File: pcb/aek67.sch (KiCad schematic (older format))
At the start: 20 parts, among them J1 AVR-ISP-6, SW1 SW_PUSH, U1 PRTR5V0U2X, U2 ATmega32U4-AU, X1 XTAL_GND

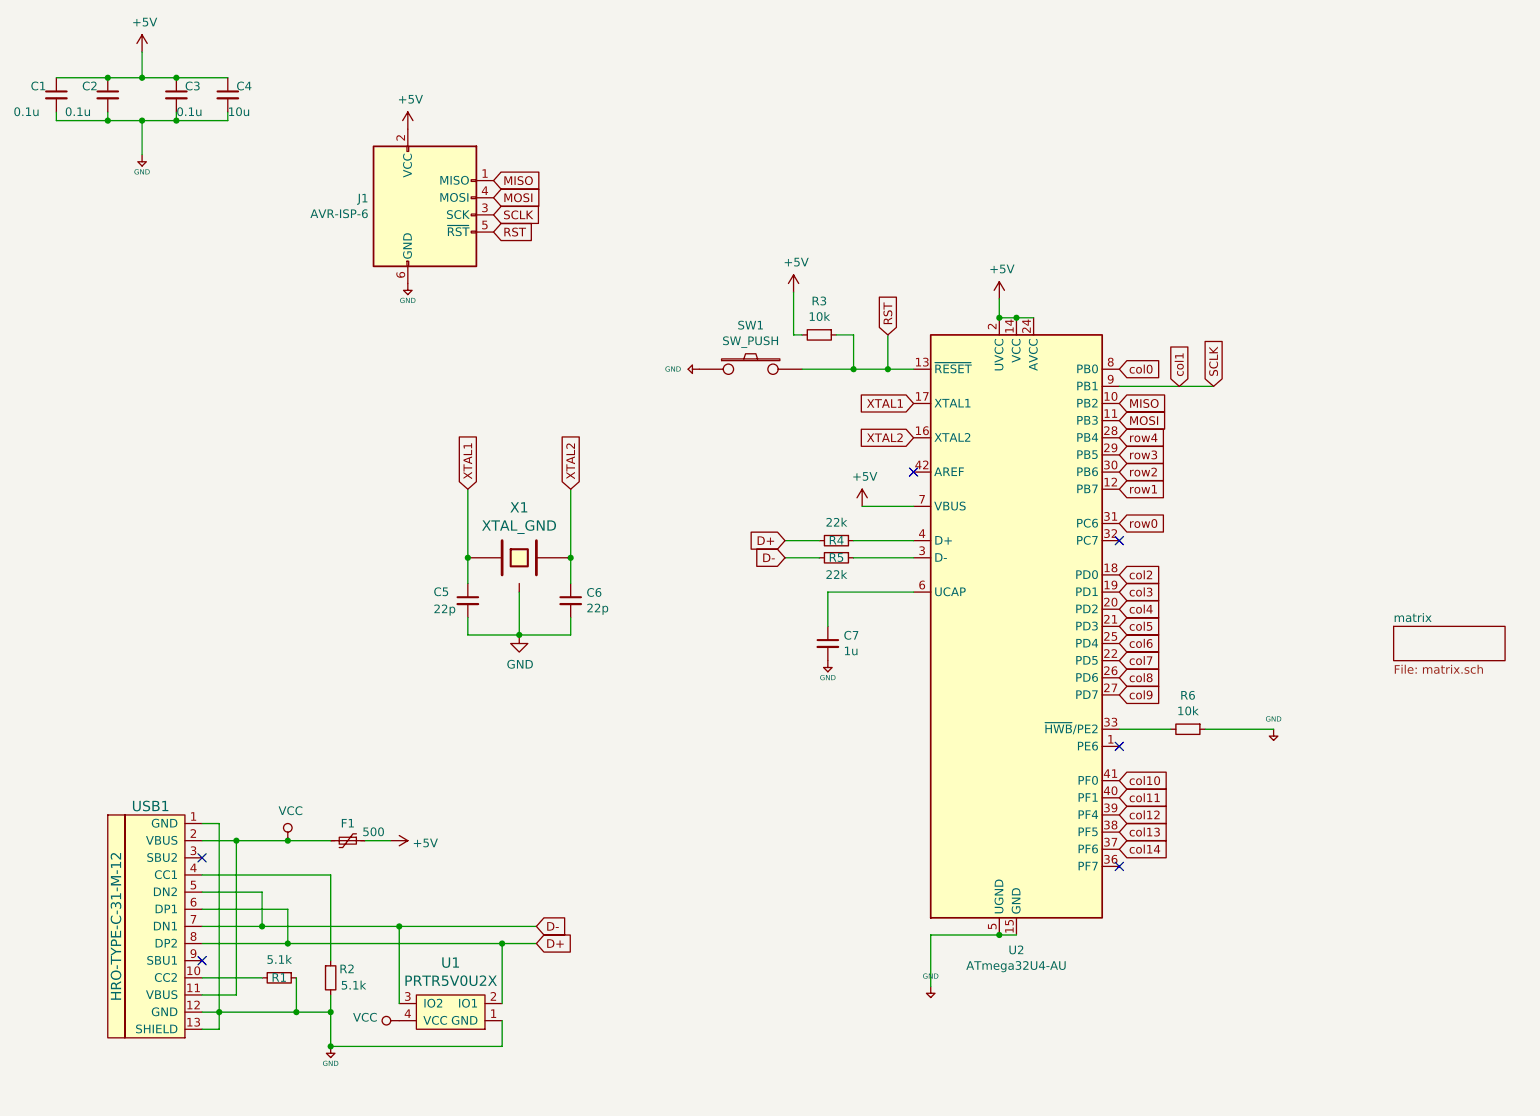
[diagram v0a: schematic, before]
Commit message: Fix GND that wasn't really a GND
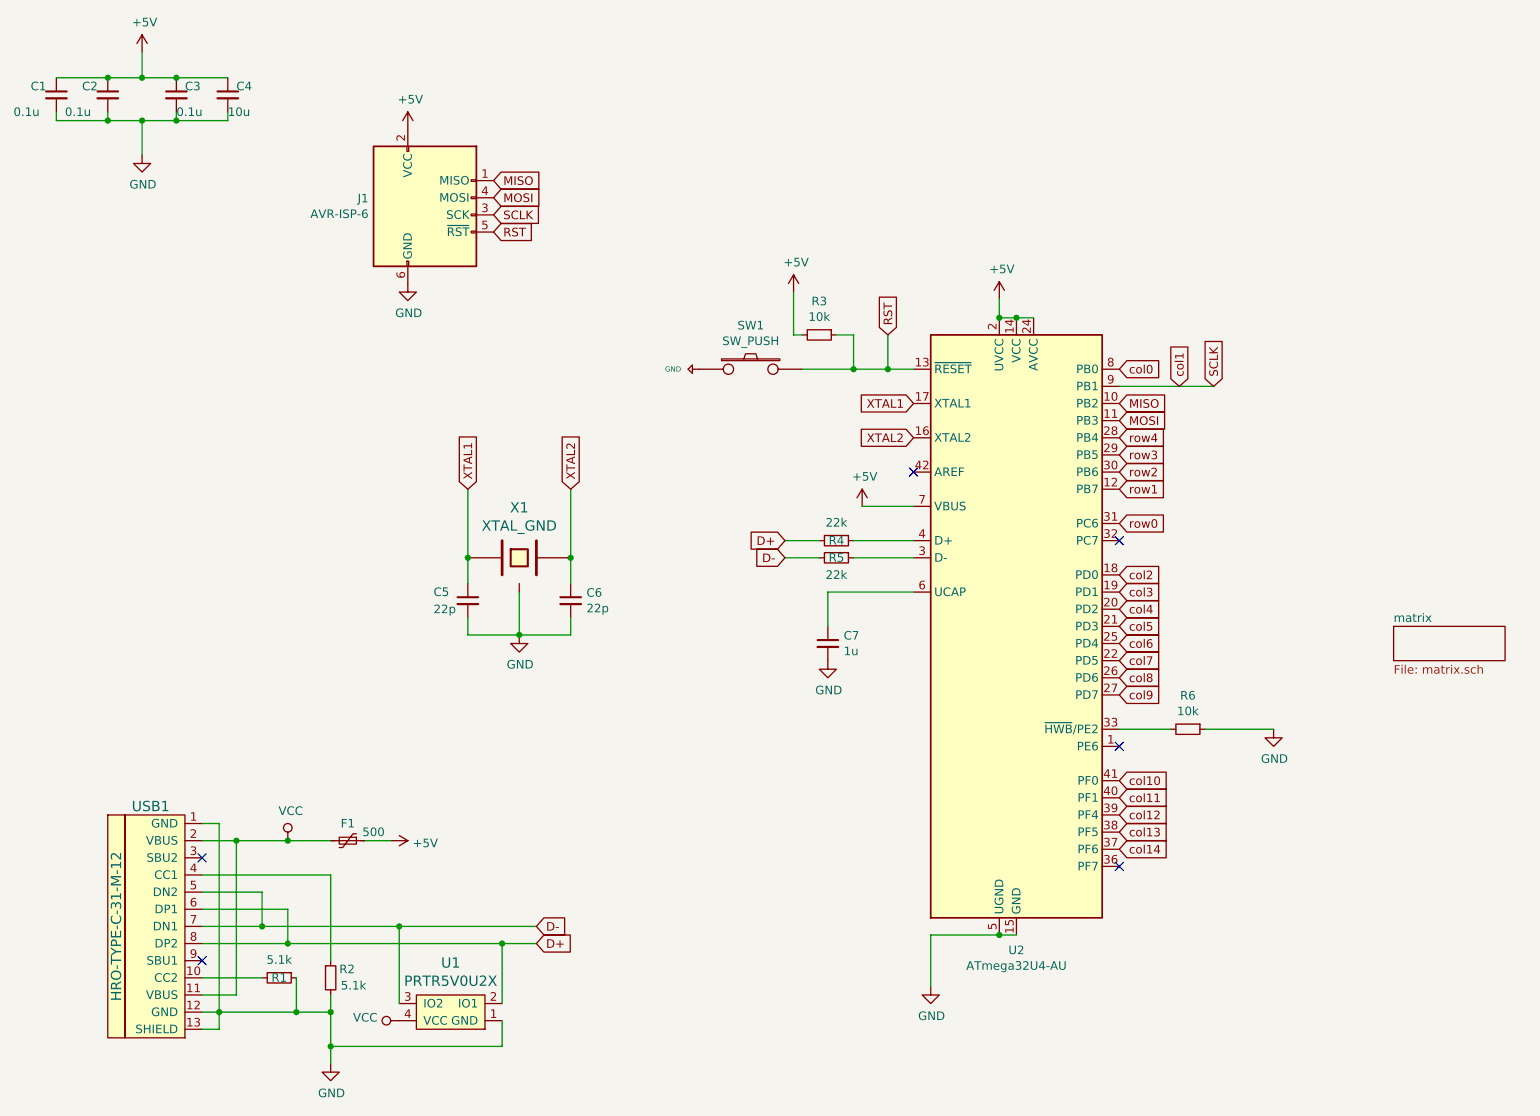
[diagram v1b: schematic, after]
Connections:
- net +5V: no longer C1.2, C2.2, C3.2, C4.2, C7.2, J1.6 (GND), R1.1, R2.2, R6.1, U1.1 (GND), U2.15 (GND), U2.23 (GND), U2.35 (GND), U2.43 (GND), U2.5 (UGND), USB1.1 (GND), USB1.12 (GND), USB1.13 (SHIELD)
- net GND: now also C1.2, C2.2, C3.2, C4.2, C7.2, J1.6 (GND), R1.1, R2.2, R6.1, U1.1 (GND), U2.15 (GND), U2.23 (GND), U2.35 (GND), U2.43 (GND), U2.5 (UGND), USB1.1 (GND), USB1.12 (GND), USB1.13 (SHIELD)
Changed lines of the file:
@@
 Wire Wire Line
 	6500 6000 6400 6000
-$Comp
-L keyboard_parts:GND #PWR013
-U 1 1 5E150234
-P 6000 6300
-F 0 "#PWR013" H 6000 6350 20  0001 C CNN
-F 1 "GND" H 6000 6359 30  0000 C CNN
-F 2 "" H 6000 6300 60  0000 C CNN
-F 3 "" H 6000 6300 60  0000 C CNN
-	1    6000 6300
-	1    0    0    -1
-$EndComp
 Wire Wire Line
 	6000 6300 6000 6000
@@
 	6000 6000 6400 6000
 Connection ~ 6400 6000
-$Comp
-L keyboard_parts:GND #PWR015
-U 1 1 5E150A49
-P 8000 4800
-F 0 "#PWR015" H 8000 4850 20  0001 C CNN
-F 1 "GND" H 8000 4859 30  0000 C CNN
-F 2 "" H 8000 4800 60  0000 C CNN
-F 3 "" H 8000 4800 60  0000 C CNN
-	1    8000 4800
-	1    0    0    -1
-$EndComp
 $Comp
 L Device:R_Small R6
@@
 $EndComp
 $Comp
-L keyboard_parts:GND #PWR02
-U 1 1 5E154981
-P 1400 1450
-F 0 "#PWR02" H 1400 1500 20  0001 C CNN
-F 1 "GND" H 1400 1350 30  0000 C CNN
-F 2 "" H 1400 1450 60  0000 C CNN
-F 3 "" H 1400 1450 60  0000 C CNN
-	1    1400 1450
-	1    0    0    -1
-$EndComp
-$Comp
 L Device:C_Small C2
 U 1 1 5E159C61
@@
 $EndComp
 $Comp
-L keyboard_parts:GND #PWR011
-U 1 1 5E17234E
-P 5400 4400
-F 0 "#PWR011" H 5400 4450 20  0001 C CNN
-F 1 "GND" H 5400 4300 30  0000 C CNN
-F 2 "" H 5400 4400 60  0000 C CNN
-F 3 "" H 5400 4400 60  0000 C CNN
-	1    5400 4400
-	1    0    0    -1
-$EndComp
-$Comp
 L Type-C:HRO-TYPE-C-31-M-12 USB1
 U 1 1 5E173F5E
@@
 	1850 6450 2300 6450
 Connection ~ 1850 6450
-$Comp
-L keyboard_parts:GND #PWR04
-U 1 1 5E17B86D
-P 2500 6650
-F 0 "#PWR04" H 2500 6700 20  0001 C CNN
-F 1 "GND" H 2500 6550 30  0000 C CNN
-F 2 "" H 2500 6650 60  0000 C CNN
-F 3 "" H 2500 6650 60  0000 C CNN
-	1    2500 6650
-	1    0    0    -1
-$EndComp
 Wire Wire Line
 	1750 6550 1850 6550
@@
 Wire Wire Line
 	3500 6650 2500 6650
-Connection ~ 2500 6650
 $Comp
 L Connector:AVR-ISP-6 J1
@@
 F 3 "" H 2950 1300 50  0001 C CNN
 	1    2950 1300
-	1    0    0    -1
-$EndComp
-$Comp
-L keyboard_parts:GND #PWR08
-U 1 1 5E1A9DF3
-P 2950 2200
-F 0 "#PWR08" H 2950 2250 20  0001 C CNN
-F 1 "GND" H 2950 2100 30  0000 C CNN
-F 2 "" H 2950 2200 60  0000 C CNN
-F 3 "" H 2950 2200 60  0000 C CNN
-	1    2950 2200
 	1    0    0    -1
 $EndComp
@@
 NoConn ~ 7100 3700
 $Comp
-L power:GND #PWR?
+L power:GND #PWR016
 U 1 1 5E3A94BD
 P 3600 4250
-F 0 "#PWR?" H 3600 4000 50  0001 C CNN
+F 0 "#PWR016" H 3600 4000 50  0001 C CNN
 F 1 "GND" H 3605 4077 50  0000 C CNN
 F 2 "" H 3600 4250 50  0001 C CNN
@@
 	1    0    0    -1
 $EndComp
+$Comp
+L power:GND #PWR013
+U 1 1 5E3AD755
+P 6000 6300
+F 0 "#PWR013" H 6000 6050 50  0001 C CNN
+F 1 "GND" H 6005 6127 50  0000 C CNN
+F 2 "" H 6000 6300 50  0001 C CNN
+F 3 "" H 6000 6300 50  0001 C CNN
+	1    6000 6300
+	1    0    0    -1
+$EndComp
+$Comp
+L power:GND #PWR015
+U 1 1 5E3ADFE1
+P 8000 4800
+F 0 "#PWR015" H 8000 4550 50  0001 C CNN
+F 1 "GND" H 8005 4627 50  0000 C CNN
+F 2 "" H 8000 4800 50  0001 C CNN
+F 3 "" H 8000 4800 50  0001 C CNN
+	1    8000 4800
+	1    0    0    -1
+$EndComp
+$Comp
+L power:GND #PWR011
+U 1 1 5E3B02F0
+P 5400 4400
+F 0 "#PWR011" H 5400 4150 50  0001 C CNN
+F 1 "GND" H 5405 4227 50  0000 C CNN
+F 2 "" H 5400 4400 50  0001 C CNN
+F 3 "" H 5400 4400 50  0001 C CNN
+	1    5400 4400
+	1    0    0    -1
+$EndComp
+$Comp
+L power:GND #PWR08
+U 1 1 5E3B07F2
+P 2950 2200
+F 0 "#PWR08" H 2950 1950 50  0001 C CNN
+F 1 "GND" H 2955 2027 50  0000 C CNN
+F 2 "" H 2950 2200 50  0001 C CNN
+F 3 "" H 2950 2200 50  0001 C CNN
+	1    2950 2200
+	1    0    0    -1
+$EndComp
+$Comp
+L power:GND #PWR02
+U 1 1 5E3B0B4C
+P 1400 1450
+F 0 "#PWR02" H 1400 1200 50  0001 C CNN
+F 1 "GND" H 1405 1277 50  0000 C CNN
+F 2 "" H 1400 1450 50  0001 C CNN
+F 3 "" H 1400 1450 50  0001 C CNN
+	1    1400 1450
+	1    0    0    -1
+$EndComp
+$Comp
+L power:GND #PWR04
+U 1 1 5E3B0FC7
+P 2500 6750
+F 0 "#PWR04" H 2500 6500 50  0001 C CNN
+F 1 "GND" H 2505 6577 50  0000 C CNN
+F 2 "" H 2500 6750 50  0001 C CNN
+F 3 "" H 2500 6750 50  0001 C CNN
+	1    2500 6750
+	1    0    0    -1
+$EndComp
+Wire Wire Line
+	2500 6650 2500 6750
+Connection ~ 2500 6650
 $EndSCHEMATC

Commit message: re-annotated everything in line instead of column
which is more clear for the matrix
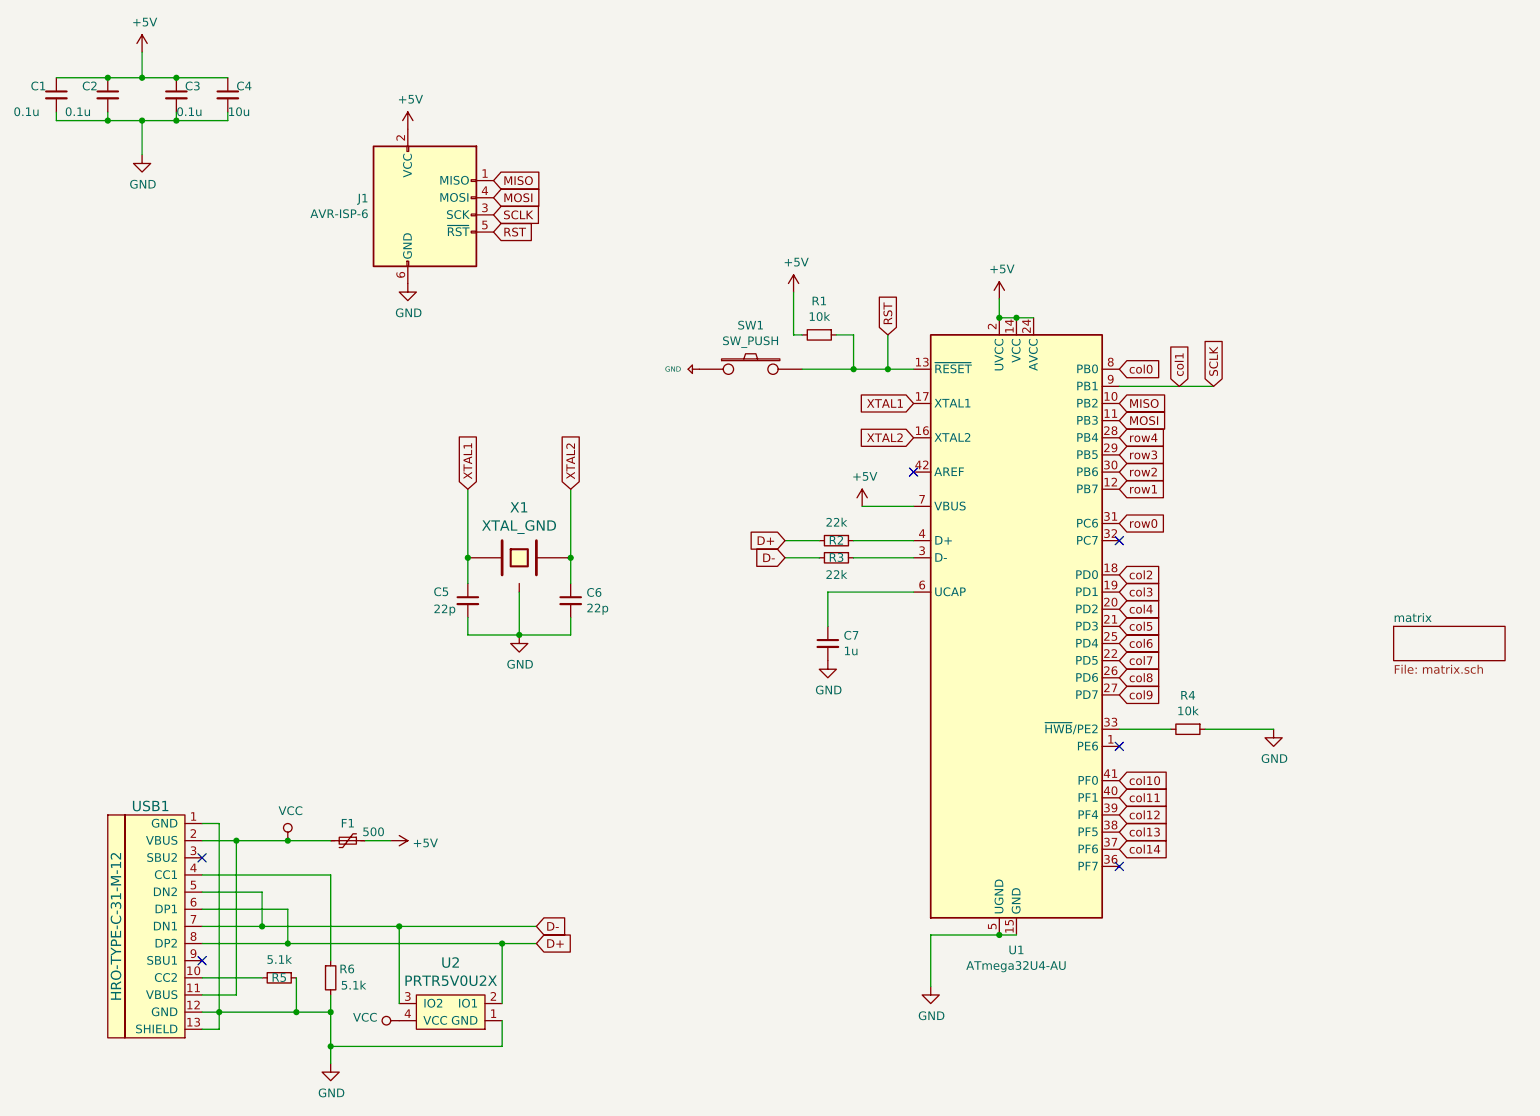
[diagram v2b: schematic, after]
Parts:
- renumbered R3 to R1, R4 to R2, R5 to R3, R6 to R4, R1 to R5, R2 to R6, U2 to U1, U1 to U2
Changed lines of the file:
@@
 $EndDescr
 $Comp
-L MCU_Microchip_ATmega:ATmega32U4-AU U2
+L MCU_Microchip_ATmega:ATmega32U4-AU U1
 U 1 1 5E07A591
 P 6500 4200
-F 0 "U2" H 6500 2311 50  0000 C CNN
+F 0 "U1" H 6500 2311 50  0000 C CNN
 F 1 "ATmega32U4-AU" H 6500 2220 50  0000 C CNN
 F 2 "Package_QFP:TQFP-44_10x10mm_P0.8mm" H 6500 4200 50  0001 C CIN
@@
 $EndComp
 $Comp
-L power:+5V #PWR014
+L power:+5V #PWR06
 U 1 1 5E14CEE1
 P 6400 2290
-F 0 "#PWR014" H 6400 2140 50  0001 C CNN
+F 0 "#PWR06" H 6400 2140 50  0001 C CNN
 F 1 "+5V" H 6415 2463 50  0000 C CNN
 F 2 "" H 6400 2290 50  0001 C CNN
@@
 Connection ~ 6400 6000
 $Comp
-L Device:R_Small R6
+L Device:R_Small R4
 U 1 1 5E15134E
 P 7500 4800
-F 0 "R6" V 7304 4800 50  0000 C CNN
+F 0 "R4" V 7304 4800 50  0000 C CNN
 F 1 "10k" V 7395 4800 50  0000 C CNN
 F 2 "Resistor_SMD:R_0805_2012Metric_Pad1.15x1.40mm_HandSolder" H 7500 4800 50  0001 C CNN
@@
 $EndComp
 $Comp
-L Device:R_Small R3
+L Device:R_Small R1
 U 1 1 5E161E9D
 P 5350 2500
-F 0 "R3" V 5154 2500 50  0000 C CNN
+F 0 "R1" V 5154 2500 50  0000 C CNN
 F 1 "10k" V 5245 2500 50  0000 C CNN
 F 2 "Resistor_SMD:R_0805_2012Metric_Pad1.15x1.40mm_HandSolder" H 5350 2500 50  0001 C CNN
@@
 	5200 2500 5200 2250
 $Comp
-L power:+5V #PWR010
+L power:+5V #PWR05
 U 1 1 5E163E07
 P 5200 2250
-F 0 "#PWR010" H 5200 2100 50  0001 C CNN
+F 0 "#PWR05" H 5200 2100 50  0001 C CNN
 F 1 "+5V" H 5215 2423 50  0000 C CNN
 F 2 "" H 5200 2250 50  0001 C CNN
@@
 $EndComp
 $Comp
-L keyboard_parts:GND #PWR09
+L keyboard_parts:GND #PWR07
 U 1 1 5E16447C
 P 4650 2700
-F 0 "#PWR09" H 4650 2750 20  0001 C CNN
+F 0 "#PWR07" H 4650 2750 20  0001 C CNN
 F 1 "GND" V 4650 2500 30  0000 L CNN
 F 2 "" H 4650 2700 60  0000 C CNN
@@
 	5550 3700 5900 3700
 $Comp
-L Device:R_Small R4
+L Device:R_Small R2
 U 1 1 5E16BFEA
 P 5450 3700
-F 0 "R4" V 5450 3700 50  0000 C CNN
+F 0 "R2" V 5450 3700 50  0000 C CNN
 F 1 "22k" V 5345 3700 50  0000 C CNN
 F 2 "Resistor_SMD:R_0805_2012Metric_Pad1.15x1.40mm_HandSolder" H 5450 3700 50  0001 C CNN
@@
 $EndComp
 $Comp
-L Device:R_Small R5
+L Device:R_Small R3
 U 1 1 5E16C54B
 P 5450 3800
-F 0 "R5" V 5450 3800 50  0000 C CNN
+F 0 "R3" V 5450 3800 50  0000 C CNN
 F 1 "22k" V 5550 3800 50  0000 C CNN
 F 2 "Resistor_SMD:R_0805_2012Metric_Pad1.15x1.40mm_HandSolder" H 5450 3800 50  0001 C CNN
@@
 	5350 3800 5150 3800
 $Comp
-L power:+5V #PWR012
+L power:+5V #PWR08
 U 1 1 5E16EF16
 P 5600 3500
-F 0 "#PWR012" H 5600 3350 50  0001 C CNN
+F 0 "#PWR08" H 5600 3350 50  0001 C CNN
 F 1 "+5V" H 5615 3673 50  0000 C CNN
 F 2 "" H 5600 3500 50  0001 C CNN
@@
 $EndComp
 $Comp
-L power:+5V #PWR05
+L power:+5V #PWR013
 U 1 1 5E177DF2
 P 2850 5450
-F 0 "#PWR05" H 2850 5300 50  0001 C CNN
+F 0 "#PWR013" H 2850 5300 50  0001 C CNN
 F 1 "+5V" V 2865 5578 50  0000 L CNN
 F 2 "" H 2850 5450 50  0001 C CNN
@@
 	2500 5650 2500 6150
 $Comp
-L Device:R_Small R2
+L Device:R_Small R6
 U 1 1 5E17FCB6
 P 2500 6250
-F 0 "R2" H 2550 6300 50  0000 L CNN
+F 0 "R6" H 2550 6300 50  0000 L CNN
 F 1 "5.1k" H 2559 6205 50  0000 L CNN
 F 2 "Resistor_SMD:R_0805_2012Metric_Pad1.15x1.40mm_HandSolder" H 2500 6250 50  0001 C CNN
@@
 	1750 6250 2100 6250
 $Comp
-L Device:R_Small R1
+L Device:R_Small R5
 U 1 1 5E1825A9
 P 2200 6250
-F 0 "R1" V 2200 6250 50  0000 C CNN
+F 0 "R5" V 2200 6250 50  0000 C CNN
 F 1 "5.1k" V 2095 6250 50  0000 C CNN
 F 2 "Resistor_SMD:R_0805_2012Metric_Pad1.15x1.40mm_HandSolder" H 2200 6250 50  0001 C CNN
@@
 Connection ~ 2250 6050
 $Comp
-L random-keyboard-parts:PRTR5V0U2X U1
+L random-keyboard-parts:PRTR5V0U2X U2
 U 1 1 5E18BDD6
 P 3200 6450
-F 0 "U1" H 3200 6163 60  0000 C CNN
+F 0 "U2" H 3200 6163 60  0000 C CNN
 F 1 "PRTR5V0U2X" H 3200 6269 60  0000 C CNN
 F 2 "local:SOT143B" H 3200 6450 60  0001 C CNN
@@
 Connection ~ 1950 5450
 $Comp
-L power:VCC #PWR03
+L power:VCC #PWR012
 U 1 1 5E1A381A
 P 2250 5450
-F 0 "#PWR03" H 2250 5300 50  0001 C CNN
+F 0 "#PWR012" H 2250 5300 50  0001 C CNN
 F 1 "VCC" H 2267 5623 50  0000 C CNN
 F 2 "" H 2250 5450 50  0001 C CNN
@@
 	2250 5450 2500 5450
 $Comp
-L power:VCC #PWR06
+L power:VCC #PWR015
 U 1 1 5E1A3F77
 P 2900 6500
-F 0 "#PWR06" H 2900 6350 50  0001 C CNN
+F 0 "#PWR015" H 2900 6350 50  0001 C CNN
 F 1 "VCC" V 2918 6627 50  0000 L CNN
 F 2 "" H 2900 6500 50  0001 C CNN
@@
 $EndComp
 $Comp
-L power:+5V #PWR07
+L power:+5V #PWR02
 U 1 1 5E1A9733
 P 2950 1300
-F 0 "#PWR07" H 2950 1150 50  0001 C CNN
+F 0 "#PWR02" H 2950 1150 50  0001 C CNN
 F 1 "+5V" H 2965 1473 50  0000 C CNN
 F 2 "" H 2950 1300 50  0001 C CNN
@@
 NoConn ~ 7100 3700
 $Comp
-L power:GND #PWR016
+L power:GND #PWR09
 U 1 1 5E3A94BD
 P 3600 4250
-F 0 "#PWR016" H 3600 4000 50  0001 C CNN
+F 0 "#PWR09" H 3600 4000 50  0001 C CNN
 F 1 "GND" H 3605 4077 50  0000 C CNN
 F 2 "" H 3600 4250 50  0001 C CNN
@@
 $EndComp
 $Comp
-L power:GND #PWR013
+L power:GND #PWR014
 U 1 1 5E3AD755
 P 6000 6300
-F 0 "#PWR013" H 6000 6050 50  0001 C CNN
+F 0 "#PWR014" H 6000 6050 50  0001 C CNN
 F 1 "GND" H 6005 6127 50  0000 C CNN
 F 2 "" H 6000 6300 50  0001 C CNN
@@
 $EndComp
 $Comp
-L power:GND #PWR015
+L power:GND #PWR011
 U 1 1 5E3ADFE1
 P 8000 4800
-F 0 "#PWR015" H 8000 4550 50  0001 C CNN
+F 0 "#PWR011" H 8000 4550 50  0001 C CNN
 F 1 "GND" H 8005 4627 50  0000 C CNN
 F 2 "" H 8000 4800 50  0001 C CNN
@@
 $EndComp
 $Comp
-L power:GND #PWR011
+L power:GND #PWR010
 U 1 1 5E3B02F0
 P 5400 4400
-F 0 "#PWR011" H 5400 4150 50  0001 C CNN
+F 0 "#PWR010" H 5400 4150 50  0001 C CNN
 F 1 "GND" H 5405 4227 50  0000 C CNN
 F 2 "" H 5400 4400 50  0001 C CNN
@@
 $EndComp
 $Comp
-L power:GND #PWR08
+L power:GND #PWR04
 U 1 1 5E3B07F2
 P 2950 2200
-F 0 "#PWR08" H 2950 1950 50  0001 C CNN
+F 0 "#PWR04" H 2950 1950 50  0001 C CNN
 F 1 "GND" H 2955 2027 50  0000 C CNN
 F 2 "" H 2950 2200 50  0001 C CNN
@@
 $EndComp
 $Comp
-L power:GND #PWR02
+L power:GND #PWR03
 U 1 1 5E3B0B4C
 P 1400 1450
-F 0 "#PWR02" H 1400 1200 50  0001 C CNN
+F 0 "#PWR03" H 1400 1200 50  0001 C CNN
 F 1 "GND" H 1405 1277 50  0000 C CNN
 F 2 "" H 1400 1450 50  0001 C CNN
@@
 $EndComp
 $Comp
-L power:GND #PWR04
+L power:GND #PWR016
 U 1 1 5E3B0FC7
 P 2500 6750
-F 0 "#PWR04" H 2500 6500 50  0001 C CNN
+F 0 "#PWR016" H 2500 6500 50  0001 C CNN
 F 1 "GND" H 2505 6577 50  0000 C CNN
 F 2 "" H 2500 6750 50  0001 C CNN
